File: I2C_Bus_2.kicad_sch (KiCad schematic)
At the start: 15 parts, among them U12 MAX-M10S, U4 BMI088, U5 LIS3MDL, U9 MS5611-01BA

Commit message: major routing update!
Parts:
- R10, R9: value 1k -> 1K
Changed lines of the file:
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@@
 			)
 		)
-		(property "Value" "1k"
+		(property "Value" "1K"
 			(at 86.106 120.65 0)
 			(effects
@@
 			)
 		)
-		(property "Value" "1k"
+		(property "Value" "1K"
 			(at 93.726 120.65 0)
 			(effects

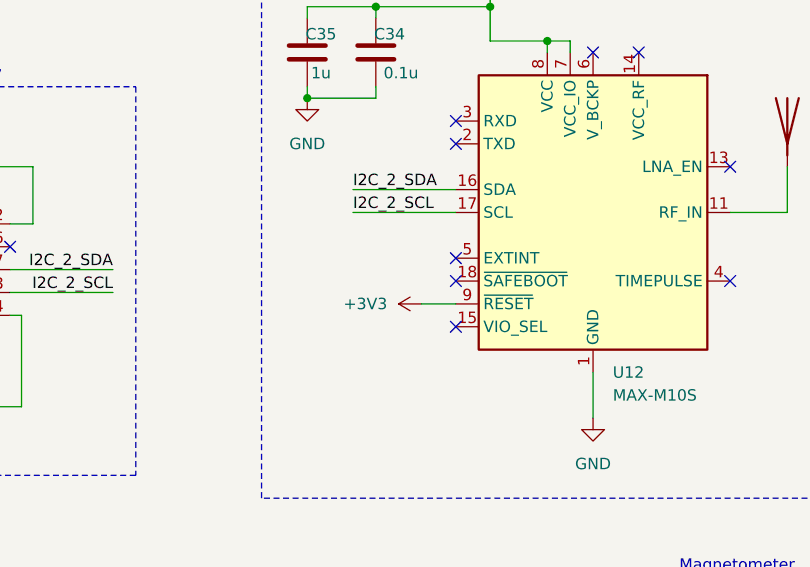
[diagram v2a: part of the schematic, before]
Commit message: Fixed PSU, routed
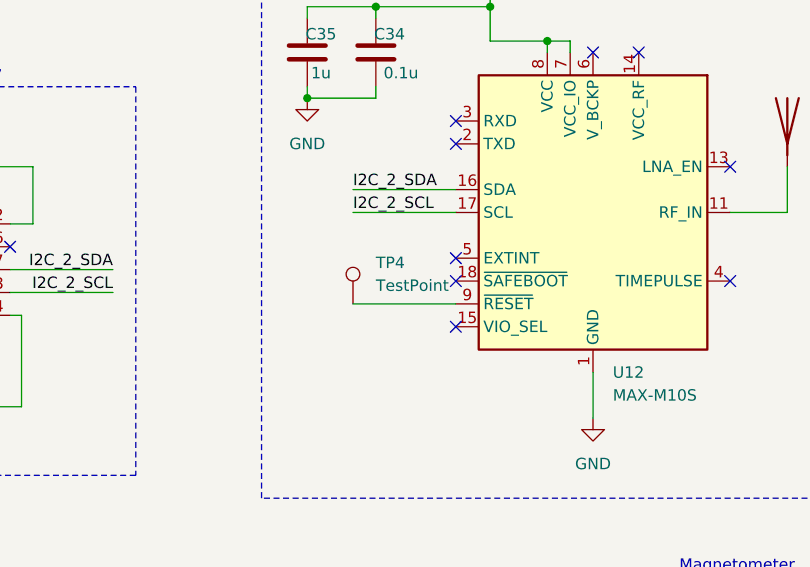
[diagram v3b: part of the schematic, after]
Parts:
- added TP4: TestPoint, TestPoint:TestPoint_Pad_D1.0mm, symbol Connector:TestPoint
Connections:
- net +3V3: no longer U12.9 (~{RESET})
- new net: TP4.1, U12.9 (~{RESET})
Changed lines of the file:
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@@
 	(wire
 		(pts
-			(xy 102.87 64.77) (xy 106.68 64.77)
+			(xy 95.25 64.77) (xy 106.68 64.77)
 		)
 		(stroke
@@
 	(symbol
 		(lib_id "power:+3V3")
-		(at 102.87 64.77 90)
-		(unit 1)
-		(exclude_from_sim no)
-		(in_bom yes)
-		(on_board yes)
-		(dnp no)
-		(fields_autoplaced yes)
-		(property "Reference" "#PWR053"
-			(at 106.68 64.77 0)
-			(effects
-				(font
-					(size 1.27 1.27)
-				)
-				(hide yes)
-			)
-		)
-		(property "Value" "+3V3"
-			(at 99.06 64.7699 90)
-			(effects
-				(font
-					(size 1.27 1.27)
-				)
-				(justify left)
-			)
-		)
-		(property "Footprint" ""
-			(at 102.87 64.77 0)
-			(effects
-				(font
-					(size 1.27 1.27)
-				)
-				(hide yes)
-			)
-		)
-		(property "Datasheet" ""
-			(at 102.87 64.77 0)
-			(effects
-				(font
-					(size 1.27 1.27)
-				)
-				(hide yes)
-			)
-		)
-		(property "Description" "Power symbol creates a global label with name \"+3V3\""
-			(at 102.87 64.77 0)
-			(effects
-				(font
-					(size 1.27 1.27)
-				)
-				(hide yes)
-			)
-		)
-		(pin "1"
-		)
-		(instances
-			(project "flight-computer-lite"
-				(path "/68fb1519-f2e0-49f5-8b7c-4cc7366600ef/b008d132-627e-4909-9b55-dae551d9f285"
-					(reference "#PWR053")
-					(unit 1)
-				)
-			)
-		)
-	)
-	(symbol
-		(lib_id "power:+3V3")
 		(at 110.49 29.21 0)
 		(unit 1)
@@
 					(unit 1)
 				)
+			)
+		)
+	)
+	(symbol
+		(lib_id "Connector:TestPoint")
+		(at 95.25 64.77 0)
+		(unit 1)
+		(exclude_from_sim no)
+		(in_bom yes)
+		(on_board yes)
+		(dnp no)
+		(fields_autoplaced yes)
+		(property "Reference" "TP4"
+			(at 97.79 60.1979 0)
+			(effects
+				(font
+					(size 1.27 1.27)
+				)
+				(justify left)
+			)
+		)
+		(property "Value" "TestPoint"
+			(at 97.79 62.7379 0)
+			(effects
+				(font
+					(size 1.27 1.27)
+				)
+				(justify left)
+			)
+		)
+		(property "Footprint" "TestPoint:TestPoint_Pad_D1.0mm"
+			(at 100.33 64.77 0)
+			(effects
+				(font
+					(size 1.27 1.27)
+				)
+				(hide yes)
+			)
+		)
+		(property "Datasheet" "~"
+			(at 100.33 64.77 0)
+			(effects
+				(font
+					(size 1.27 1.27)
+				)
+				(hide yes)
+			)
+		)
+		(property "Description" "test point"
+			(at 95.25 64.77 0)
+			(effects
+				(font
+					(size 1.27 1.27)
+				)
+				(hide yes)
+			)
+		)
+		(pin "1"
+		)
+		(instances
+			(project "flight-computer-lite"
+				(path "/68fb1519-f2e0-49f5-8b7c-4cc7366600ef/b008d132-627e-4909-9b55-dae551d9f285"
+					(reference "TP4")
+					(unit 1)
+				)
